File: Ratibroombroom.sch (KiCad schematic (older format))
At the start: 96 parts, among them J1 Conn_01x02_Male, J10 Conn_01x04_Male, J11 Conn_01x04_Male, J2 Conn_01x02_Male, J3 Conn_01x04_Male, J4 Conn_01x04_Male, J5 Conn_01x02_Male, J6 Conn_01x02_Male, J7 Conn_01x04_Male, J8 Conn_01x04_Male, J9 Conn_01x04_Male, Q1 IRLML6344, Q10 Q_NPN_BEC, Q2 IRLML6344, Q3 IRLML6344, Q4 IRLML6344, Q5 PT12-21B/TR8, Q6 PT12-21B/TR8, Q7 PT12-21B/TR8, Q8 PT12-21B/TR8, Q9 IRLML6344, SW1 B3U, SW2 B3U, U1 AZ1117-3.3, U2 DRV8835, U3 AS5145B-HSST, U4 MPU-9250, U5 STM32F405RGTx, U6 AS5145B-HSST, U7 DRV8835, Y1 8MHZ

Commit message: Add linear regulators to motor drivers supply. Include jumpers to select between direct (battery), regulated or none supply for the drivers.
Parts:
- added C28, C29, C30, C31: 10u, Capacitor_SMD:C_0603_1608Metric, symbol Device:C
- added JP1, JP2: Jumper_NC_Dual, Jumper:SolderJumper-3_P1.3mm_Open_RoundedPad1.0x1.5mm_NumberLabels, symbol Device:Jumper_NC_Dual
- added R28, R30: 5.6k, Resistor_SMD:R_0603_1608Metric, symbol Device:R
- added R29, R31: 1.8k, Resistor_SMD:R_0603_1608Metric, symbol Device:R
- added U8, U9: L6932D1.2TR, Package_SO:SO-8_5.3x6.2mm_P1.27mm, symbol schematic_sybmols:L6932D1.2TR
- C1, C10, C11, C12, C13, C14, C15, C16, C17, C18, C19, C2, C20, C21, C22, C23, C24, C25, C26, C27, C3, C4, C5, C6, C7, C8, C9: footprint (none) -> Capacitor_SMD:C_0603_1608Metric
- D1, D10, D7, D8, D9: footprint (none) -> LED_SMD:LED_0603_1608Metric
- R1, R10, R11, R12, R13, R14, R15, R16, R17, R18, R19, R2, R20, R21, R22, R23, R24, R25, R26, R27, R3, R4, R5, R6, R7, R8, R9: footprint (none) -> Resistor_SMD:R_0603_1608Metric
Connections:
- net labels added: FAN_MOTOR_1, FAN_MOTOR_2, V_MOTOR_L, V_MOTOR_R
- wire segments 343 -> 411
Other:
- moved on the sheet: C11, C12, C13, C14, C15, C16, C17, C18, C19, C20, C21, C22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

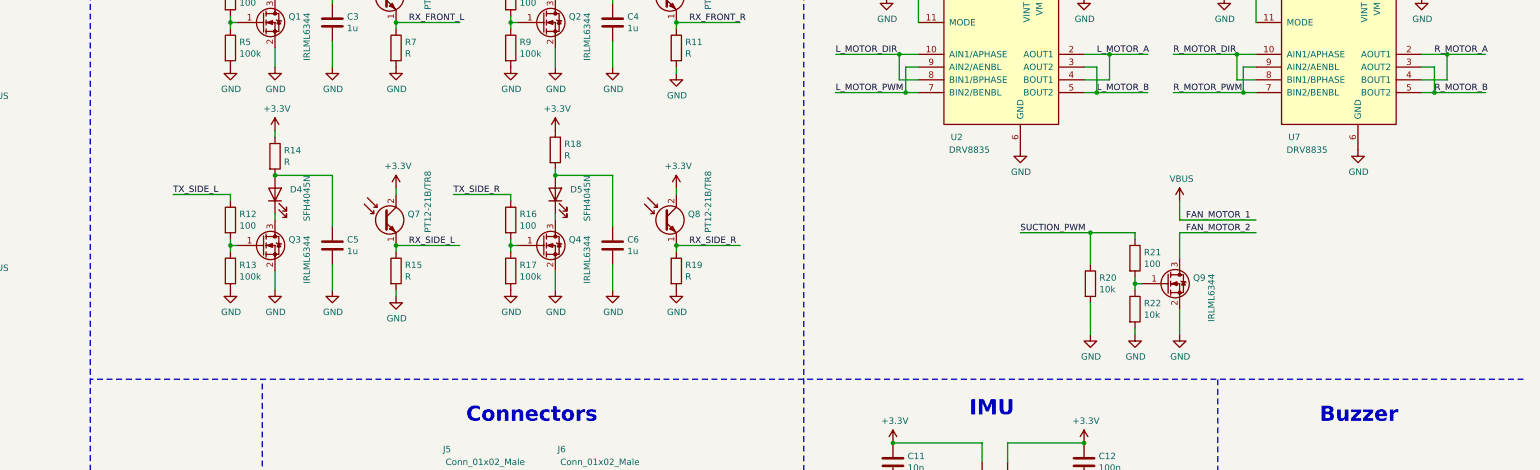
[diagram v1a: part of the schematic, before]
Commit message: Added pull-down resistors on motor pwm lines
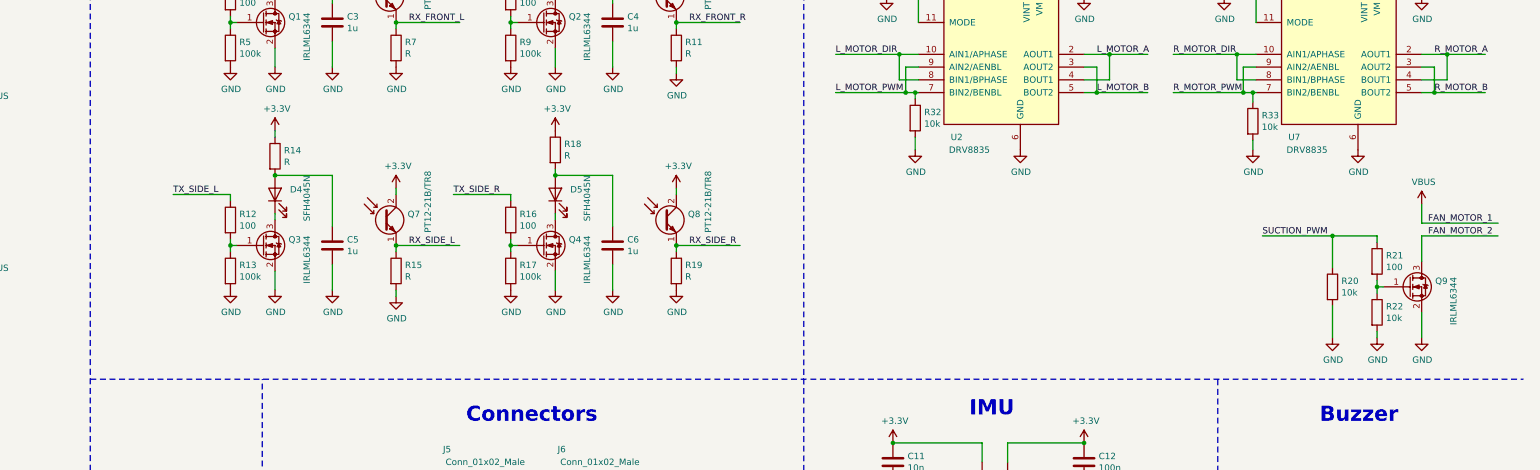
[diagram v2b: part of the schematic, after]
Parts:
- added R32, R33: 10k, Resistor_SMD:R_0603_1608Metric, symbol Device:R
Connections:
- wire segments 411 -> 417
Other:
- moved on the sheet: Q9, R20, R21, R22
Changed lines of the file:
@@
 EESchema Schematic File Version 4
 LIBS:Ratibroombroom-cache
-EELAYER 29 0
+EELAYER 26 0
 EELAYER END
 $Descr A3 16535 11693
@@
 L power:GND #PWR056
 U 1 1 5E51EE62
-P 12950 4300
-F 0 "#PWR056" H 12950 4050 50  0001 C CNN
-F 1 "GND" H 12955 4127 50  0000 C CNN
-F 2 "" H 12950 4300 50  0001 C CNN
-F 3 "" H 12950 4300 50  0001 C CNN
-	1    12950 4300
+P 14850 4325
+F 0 "#PWR056" H 14850 4075 50  0001 C CNN
+F 1 "GND" H 14855 4152 50  0000 C CNN
+F 2 "" H 14850 4325 50  0001 C CNN
+F 3 "" H 14850 4325 50  0001 C CNN
+	1    14850 4325
 	1    0    0    -1
 $EndComp
 Wire Wire Line
-	12950 3550 12950 3500
-Text Label 12050 3500 0    50   ~ 0
+	14850 3575 14850 3525
+Text Label 13950 3525 0    50   ~ 0
 SUCTION_PWM
 Wire Wire Line
-	12950 3900 12950 3850
-Connection ~ 12950 3900
+	14850 3925 14850 3875
+Connection ~ 14850 3925
 Wire Wire Line
-	13000 3900 12950 3900
+	14900 3925 14850 3925
 Wire Wire Line
-	12950 3950 12950 3900
+	14850 3975 14850 3925
 Wire Wire Line
-	13300 4100 13300 4300
+	15200 4125 15200 4325
 $Comp
 L power:GND #PWR058
 U 1 1 5E51EE81
-P 13300 4300
-F 0 "#PWR058" H 13300 4050 50  0001 C CNN
-F 1 "GND" H 13305 4127 50  0000 C CNN
-F 2 "" H 13300 4300 50  0001 C CNN
-F 3 "" H 13300 4300 50  0001 C CNN
-	1    13300 4300
+P 15200 4325
+F 0 "#PWR058" H 15200 4075 50  0001 C CNN
+F 1 "GND" H 15205 4152 50  0000 C CNN
+F 2 "" H 15200 4325 50  0001 C CNN
+F 3 "" H 15200 4325 50  0001 C CNN
+	1    15200 4325
 	1    0    0    -1
 $EndComp
@@
 L Device:R R21
 U 1 1 5E51EE8B
-P 12950 3700
-F 0 "R21" H 13020 3746 50  0000 L CNN
-F 1 "100" H 13020 3655 50  0000 L CNN
-F 2 "Resistor_SMD:R_0603_1608Metric" V 12880 3700 50  0001 C CNN
-F 3 "~" H 12950 3700 50  0001 C CNN
-	1    12950 3700
+P 14850 3725
+F 0 "R21" H 14920 3771 50  0000 L CNN
+F 1 "100" H 14920 3680 50  0000 L CNN
+F 2 "Resistor_SMD:R_0603_1608Metric" V 14780 3725 50  0001 C CNN
+F 3 "~" H 14850 3725 50  0001 C CNN
+	1    14850 3725
 	1    0    0    -1
 $EndComp
@@
 L Device:R R22
 U 1 1 5E51EE95
-P 12950 4100
-F 0 "R22" H 13020 4146 50  0000 L CNN
-F 1 "10k" H 13020 4055 50  0000 L CNN
-F 2 "Resistor_SMD:R_0603_1608Metric" V 12880 4100 50  0001 C CNN
-F 3 "~" H 12950 4100 50  0001 C CNN
-	1    12950 4100
+P 14850 4125
+F 0 "R22" H 14920 4171 50  0000 L CNN
+F 1 "10k" H 14920 4080 50  0000 L CNN
+F 2 "Resistor_SMD:R_0603_1608Metric" V 14780 4125 50  0001 C CNN
+F 3 "~" H 14850 4125 50  0001 C CNN
+	1    14850 4125
 	1    0    0    -1
 $EndComp
@@
 L Device:Q_NMOS_GSD Q9
 U 1 1 5E51EE9F
-P 13200 3900
-F 0 "Q9" H 13406 3946 50  0000 L CNN
-F 1 "IRLML6344" V 13550 3600 50  0000 L CNN
-F 2 "" H 13400 4000 50  0001 C CNN
-F 3 "~" H 13200 3900 50  0001 C CNN
-	1    13200 3900
+P 15100 3925
+F 0 "Q9" H 15306 3971 50  0000 L CNN
+F 1 "IRLML6344" V 15450 3625 50  0000 L CNN
+F 2 "" H 15300 4025 50  0001 C CNN
+F 3 "~" H 15100 3925 50  0001 C CNN
+	1    15100 3925
 	1    0    0    -1
 $EndComp
@@
 $EndComp
 Wire Wire Line
-	13900 3500 13300 3500
+	15800 3525 15200 3525
 Wire Wire Line
-	13300 3500 13300 3700
+	15200 3525 15200 3725
 Wire Wire Line
-	13900 3400 13300 3400
+	15800 3425 15200 3425
 Wire Wire Line
-	13300 3400 13300 3250
+	15200 3425 15200 3275
 $Comp
 L power:VBUS #PWR057
 U 1 1 5E53C651
-P 13300 3250
-F 0 "#PWR057" H 13300 3100 50  0001 C CNN
-F 1 "VBUS" H 13315 3423 50  0000 C CNN
-F 2 "" H 13300 3250 50  0001 C CNN
-F 3 "" H 13300 3250 50  0001 C CNN
-	1    13300 3250
+P 15200 3275
+F 0 "#PWR057" H 15200 3125 50  0001 C CNN
+F 1 "VBUS" H 15215 3448 50  0000 C CNN
+F 2 "" H 15200 3275 50  0001 C CNN
+F 3 "" H 15200 3275 50  0001 C CNN
+	1    15200 3275
 	1    0    0    -1
 $EndComp
@@
 L Device:R R20
 U 1 1 5E53FDF5
-P 12600 3900
-F 0 "R20" H 12670 3946 50  0000 L CNN
-F 1 "10k" H 12670 3855 50  0000 L CNN
-F 2 "Resistor_SMD:R_0603_1608Metric" V 12530 3900 50  0001 C CNN
-F 3 "~" H 12600 3900 50  0001 C CNN
-	1    12600 3900
+P 14500 3925
+F 0 "R20" H 14570 3971 50  0000 L CNN
+F 1 "10k" H 14570 3880 50  0000 L CNN
+F 2 "Resistor_SMD:R_0603_1608Metric" V 14430 3925 50  0001 C CNN
+F 3 "~" H 14500 3925 50  0001 C CNN
+	1    14500 3925
 	1    0    0    -1
 $EndComp
@@
 L power:GND #PWR055
 U 1 1 5E5400FA
-P 12600 4300
-F 0 "#PWR055" H 12600 4050 50  0001 C CNN
-F 1 "GND" H 12605 4127 50  0000 C CNN
-F 2 "" H 12600 4300 50  0001 C CNN
-F 3 "" H 12600 4300 50  0001 C CNN
-	1    12600 4300
+P 14500 4325
+F 0 "#PWR055" H 14500 4075 50  0001 C CNN
+F 1 "GND" H 14505 4152 50  0000 C CNN
+F 2 "" H 14500 4325 50  0001 C CNN
+F 3 "" H 14500 4325 50  0001 C CNN
+	1    14500 4325
 	1    0    0    -1
 $EndComp
-Wire Wire Line
-	12050 3500 12600 3500
-Wire Wire Line
-	12600 3750 12600 3500
-Connection ~ 12600 3500
-Wire Wire Line
-	12600 3500 12950 3500
 $Comp
 L Device:LED D7
@@
 	7150 3950 7150 4000
 Wire Wire Line
-	12950 4250 12950 4300
+	14850 4275 14850 4325
 Wire Wire Line
-	12600 4050 12600 4300
+	14500 4075 14500 4325
 $Comp
 L Connector:Conn_01x04_Male J7
@@
 Wire Wire Line
 	9250 7250 8700 7250
-Text Label 13350 3400 0    50   ~ 0
+Text Label 15250 3425 0    50   ~ 0
 FAN_MOTOR_1
-Text Label 13350 3500 0    50   ~ 0
+Text Label 15250 3525 0    50   ~ 0
 FAN_MOTOR_2
 $Comp
@@
 	11150 2200 11150 2400
 Wire Wire Line
-	11150 2400 11250 2400
+	11150 2400 11225 2400
 Wire Wire Line
 	11150 2400 10600 2400
@@
 	13800 2200 13800 2400
 Wire Wire Line
-	13800 2400 13900 2400
+	13800 2400 13875 2400
 Wire Wire Line
 	13800 2400 13250 2400
 Connection ~ 13800 2400
 Wire Notes Line width 12
-	16000 4650 10350 4650
-Wire Notes Line width 12
 	10350 7450 16050 7450
 Wire Notes Line width 12
@@
 	10350 500  10350 11200
 Wire Notes Line
-	10350 4650 4750 4650
-Wire Notes Line
 	4750 5450 500  5450
 Wire Notes Line
@@
 Wire Notes Line
 	6100 8650 6100 4650
+Wire Notes Line
+	4750 4650 16000 4650
+Wire Wire Line
+	14500 3775 14500 3525
+Connection ~ 14500 3525
+Wire Wire Line
+	14500 3525 14850 3525
+Wire Wire Line
+	13950 3525 14500 3525
+$Comp
+L Device:R R33
+U 1 1 5E2DCD69
+P 13875 2625
+F 0 "R33" H 13945 2671 50  0000 L CNN
+F 1 "10k" H 13945 2580 50  0000 L CNN
+F 2 "Resistor_SMD:R_0603_1608Metric" V 13805 2625 50  0001 C CNN
+F 3 "~" H 13875 2625 50  0001 C CNN
+	1    13875 2625
+	1    0    0    -1
+$EndComp
+$Comp
+L Device:R R32
+U 1 1 5E2DCFAB
+P 11225 2600
+F 0 "R32" H 11295 2646 50  0000 L CNN
+F 1 "10k" H 11295 2555 50  0000 L CNN
+F 2 "Resistor_SMD:R_0603_1608Metric" V 11155 2600 50  0001 C CNN
+F 3 "~" H 11225 2600 50  0001 C CNN
+	1    11225 2600
+	1    0    0    -1
+$EndComp
+$Comp
+L power:GND #PWR092
+U 1 1 5E2DD0D3
+P 13875 2850
+F 0 "#PWR092" H 13875 2600 50  0001 C CNN
+F 1 "GND" H 13880 2677 50  0000 C CNN
+F 2 "" H 13875 2850 50  0001 C CNN
+F 3 "" H 13875 2850 50  0001 C CNN
+	1    13875 2850
+	1    0    0    -1
+$EndComp
+$Comp
+L power:GND #PWR091
+U 1 1 5E2DD1BA
+P 11225 2850
+F 0 "#PWR091" H 11225 2600 50  0001 C CNN
+F 1 "GND" H 11230 2677 50  0000 C CNN
+F 2 "" H 11225 2850 50  0001 C CNN
+F 3 "" H 11225 2850 50  0001 C CNN
+	1    11225 2850
+	1    0    0    -1
+$EndComp
+Wire Wire Line
+	11225 2450 11225 2400
+Connection ~ 11225 2400
+Wire Wire Line
+	11225 2400 11250 2400
+Wire Wire Line
+	11225 2750 11225 2850
+Wire Wire Line
+	13875 2475 13875 2400
+Connection ~ 13875 2400
+Wire Wire Line
+	13875 2400 13900 2400
+Wire Wire Line
+	13875 2850 13875 2775
 $EndSCHEMATC

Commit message: Added comments in schematics
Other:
- note added: "C3, C4, C5, C6\nteñen que ir ahí \nou a 3V3.\nComentar"
- note added: "Engadín R32 e R33 para que\nen caso de 3º estado os nos \npines do micro, non se activen\nos motores"
- note added: "JP1 e JP2:\nse poden quedar\nabertos, valen \npara desconectar\nmotores"
- note added: "Por qué?"
- note added: "R28, R29, R30, R31\nque sexan do 1% \nou mellor para que\nnon se desbalanceen\nas tensións dos motores"
- moved on the sheet: Q9, R20, R21, R22
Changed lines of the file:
@@
 L power:GND #PWR056
 U 1 1 5E51EE62
-P 14850 4325
-F 0 "#PWR056" H 14850 4075 50  0001 C CNN
-F 1 "GND" H 14855 4152 50  0000 C CNN
-F 2 "" H 14850 4325 50  0001 C CNN
-F 3 "" H 14850 4325 50  0001 C CNN
-	1    14850 4325
-	1    0    0    -1
-$EndComp
-Wire Wire Line
-	14850 3575 14850 3525
-Text Label 13950 3525 0    50   ~ 0
+P 13000 4300
+F 0 "#PWR056" H 13000 4050 50  0001 C CNN
+F 1 "GND" H 13005 4127 50  0000 C CNN
+F 2 "" H 13000 4300 50  0001 C CNN
+F 3 "" H 13000 4300 50  0001 C CNN
+	1    13000 4300
+	1    0    0    -1
+$EndComp
+Wire Wire Line
+	13000 3550 13000 3500
+Text Label 12100 3500 0    50   ~ 0
 SUCTION_PWM
 Wire Wire Line
-	14850 3925 14850 3875
-Connection ~ 14850 3925
-Wire Wire Line
-	14900 3925 14850 3925
-Wire Wire Line
-	14850 3975 14850 3925
-Wire Wire Line
-	15200 4125 15200 4325
+	13000 3900 13000 3850
+Connection ~ 13000 3900
+Wire Wire Line
+	13050 3900 13000 3900
+Wire Wire Line
+	13000 3950 13000 3900
+Wire Wire Line
+	13350 4100 13350 4300
 $Comp
 L power:GND #PWR058
 U 1 1 5E51EE81
-P 15200 4325
-F 0 "#PWR058" H 15200 4075 50  0001 C CNN
-F 1 "GND" H 15205 4152 50  0000 C CNN
-F 2 "" H 15200 4325 50  0001 C CNN
-F 3 "" H 15200 4325 50  0001 C CNN
-	1    15200 4325
+P 13350 4300
+F 0 "#PWR058" H 13350 4050 50  0001 C CNN
+F 1 "GND" H 13355 4127 50  0000 C CNN
+F 2 "" H 13350 4300 50  0001 C CNN
+F 3 "" H 13350 4300 50  0001 C CNN
+	1    13350 4300
 	1    0    0    -1
 $EndComp
@@
 L Device:R R21
 U 1 1 5E51EE8B
-P 14850 3725
-F 0 "R21" H 14920 3771 50  0000 L CNN
-F 1 "100" H 14920 3680 50  0000 L CNN
-F 2 "Resistor_SMD:R_0603_1608Metric" V 14780 3725 50  0001 C CNN
-F 3 "~" H 14850 3725 50  0001 C CNN
-	1    14850 3725
+P 13000 3700
+F 0 "R21" H 13070 3746 50  0000 L CNN
+F 1 "100" H 13070 3655 50  0000 L CNN
+F 2 "Resistor_SMD:R_0603_1608Metric" V 12930 3700 50  0001 C CNN
+F 3 "~" H 13000 3700 50  0001 C CNN
+	1    13000 3700
 	1    0    0    -1
 $EndComp
@@
 L Device:R R22
 U 1 1 5E51EE95
-P 14850 4125
-F 0 "R22" H 14920 4171 50  0000 L CNN
-F 1 "10k" H 14920 4080 50  0000 L CNN
-F 2 "Resistor_SMD:R_0603_1608Metric" V 14780 4125 50  0001 C CNN
-F 3 "~" H 14850 4125 50  0001 C CNN
-	1    14850 4125
+P 13000 4100
+F 0 "R22" H 13070 4146 50  0000 L CNN
+F 1 "10k" H 13070 4055 50  0000 L CNN
+F 2 "Resistor_SMD:R_0603_1608Metric" V 12930 4100 50  0001 C CNN
+F 3 "~" H 13000 4100 50  0001 C CNN
+	1    13000 4100
 	1    0    0    -1
 $EndComp
@@
 L Device:Q_NMOS_GSD Q9
 U 1 1 5E51EE9F
-P 15100 3925
-F 0 "Q9" H 15306 3971 50  0000 L CNN
-F 1 "IRLML6344" V 15450 3625 50  0000 L CNN
-F 2 "" H 15300 4025 50  0001 C CNN
-F 3 "~" H 15100 3925 50  0001 C CNN
-	1    15100 3925
+P 13250 3900
+F 0 "Q9" H 13456 3946 50  0000 L CNN
+F 1 "IRLML6344" V 13600 3600 50  0000 L CNN
+F 2 "" H 13450 4000 50  0001 C CNN
+F 3 "~" H 13250 3900 50  0001 C CNN
+	1    13250 3900
 	1    0    0    -1
 $EndComp
@@
 $EndComp
 Wire Wire Line
-	15800 3525 15200 3525
-Wire Wire Line
-	15200 3525 15200 3725
-Wire Wire Line
-	15800 3425 15200 3425
-Wire Wire Line
-	15200 3425 15200 3275
+	13950 3500 13350 3500
+Wire Wire Line
+	13350 3500 13350 3700
+Wire Wire Line
+	13950 3400 13350 3400
+Wire Wire Line
+	13350 3400 13350 3250
 $Comp
 L power:VBUS #PWR057
 U 1 1 5E53C651
-P 15200 3275
-F 0 "#PWR057" H 15200 3125 50  0001 C CNN
-F 1 "VBUS" H 15215 3448 50  0000 C CNN
-F 2 "" H 15200 3275 50  0001 C CNN
-F 3 "" H 15200 3275 50  0001 C CNN
-	1    15200 3275
+P 13350 3250
+F 0 "#PWR057" H 13350 3100 50  0001 C CNN
+F 1 "VBUS" H 13365 3423 50  0000 C CNN
+F 2 "" H 13350 3250 50  0001 C CNN
+F 3 "" H 13350 3250 50  0001 C CNN
+	1    13350 3250
 	1    0    0    -1
 $EndComp
@@
 L Device:R R20
 U 1 1 5E53FDF5
-P 14500 3925
-F 0 "R20" H 14570 3971 50  0000 L CNN
-F 1 "10k" H 14570 3880 50  0000 L CNN
-F 2 "Resistor_SMD:R_0603_1608Metric" V 14430 3925 50  0001 C CNN
-F 3 "~" H 14500 3925 50  0001 C CNN
-	1    14500 3925
+P 12650 3900
+F 0 "R20" H 12720 3946 50  0000 L CNN
+F 1 "10k" H 12720 3855 50  0000 L CNN
+F 2 "Resistor_SMD:R_0603_1608Metric" V 12580 3900 50  0001 C CNN
+F 3 "~" H 12650 3900 50  0001 C CNN
+	1    12650 3900
 	1    0    0    -1
 $EndComp
@@
 L power:GND #PWR055
 U 1 1 5E5400FA
-P 14500 4325
-F 0 "#PWR055" H 14500 4075 50  0001 C CNN
-F 1 "GND" H 14505 4152 50  0000 C CNN
-F 2 "" H 14500 4325 50  0001 C CNN
-F 3 "" H 14500 4325 50  0001 C CNN
-	1    14500 4325
+P 12650 4300
+F 0 "#PWR055" H 12650 4050 50  0001 C CNN
+F 1 "GND" H 12655 4127 50  0000 C CNN
+F 2 "" H 12650 4300 50  0001 C CNN
+F 3 "" H 12650 4300 50  0001 C CNN
+	1    12650 4300
 	1    0    0    -1
 $EndComp
@@
 	7150 3950 7150 4000
 Wire Wire Line
-	14850 4275 14850 4325
-Wire Wire Line
-	14500 4075 14500 4325
+	13000 4250 13000 4300
+Wire Wire Line
+	12650 4050 12650 4300
 $Comp
 L Connector:Conn_01x04_Male J7
@@
 Wire Wire Line
 	9250 7250 8700 7250
-Text Label 15250 3425 0    50   ~ 0
+Text Label 13400 3400 0    50   ~ 0
 FAN_MOTOR_1
-Text Label 15250 3525 0    50   ~ 0
+Text Label 13400 3500 0    50   ~ 0
 FAN_MOTOR_2
 $Comp
@@
 	4750 4650 16000 4650
 Wire Wire Line
-	14500 3775 14500 3525
-Connection ~ 14500 3525
-Wire Wire Line
-	14500 3525 14850 3525
-Wire Wire Line
-	13950 3525 14500 3525
+	12650 3750 12650 3500
+Connection ~ 12650 3500
+Wire Wire Line
+	12650 3500 13000 3500
+Wire Wire Line
+	12100 3500 12650 3500
 $Comp
 L Device:R R33
@@
 Wire Wire Line
 	13875 2850 13875 2775
+Text Notes 3800 3650 0    50   ~ 0
+R28, R29, R30, R31\nque sexan do 1% \nou mellor para que\nnon se desbalanceen\nas tensións dos motores
+Text Notes 875  2975 0    50   ~ 0
+JP1 e JP2:\nse poden quedar\nabertos, valen \npara desconectar\nmotores
+Text Notes 6800 2825 0    50   ~ 0
+C3, C4, C5, C6\nteñen que ir ahí \nou a 3V3.\nComentar
+Text Notes 12475 2875 0    50   ~ 0
+Engadín R32 e R33 para que\nen caso de 3º estado os nos \npines do micro, non se activen\nos motores
+Text Notes 3875 8675 0    50   ~ 0
+Por qué?
 $EndSCHEMATC

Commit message: More comments on schematics
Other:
- note added: "Comentar cómo se vai\na integrar a PCB principal\ncoas dos encoders"
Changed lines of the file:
@@
 Text Notes 3875 8675 0    50   ~ 0
 Por qué?
+Text Notes 10000 8275 0    50   ~ 0
+Comentar cómo se vai\na integrar a PCB principal\ncoas dos encoders
 $EndSCHEMATC

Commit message: Typo fix
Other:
- note added: "Engadín R32 e R33 para que\nen caso de 3º estado nos \npines do micro, non se activen\nos motores"
- note removed: "Engadín R32 e R33 para que\nen caso de 3º estado os nos \npines do micro, non se activen\nos motores"
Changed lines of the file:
@@
 C3, C4, C5, C6\nteñen que ir ahí \nou a 3V3.\nComentar
 Text Notes 12475 2875 0    50   ~ 0
-Engadín R32 e R33 para que\nen caso de 3º estado os nos \npines do micro, non se activen\nos motores
+Engadín R32 e R33 para que\nen caso de 3º estado nos \npines do micro, non se activen\nos motores
 Text Notes 3875 8675 0    50   ~ 0
 Por qué?

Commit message: Modify connection of capacitors in IR emitters. Add on/of switch through mosfet. Assign footprints to every schematic symbol.
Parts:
- added Q11: IRF7416PbF, Package_SO:SO-8_5.3x6.2mm_P1.27mm, symbol schematic_sybmols:IRF7416PbF
- added R34: 10k, Resistor_SMD:R_0603_1608Metric, symbol Device:R
- added SW3: PCM12, Button_Switch_SMD:SW_SPDT_PCM12, symbol Switch:SW_DPDT_x2
- BZ1: footprint (none) -> Ratibroombroom:MLT-5020
- D2, D3, D4, D5: footprint (none) -> Ratibroombroom:SFH4045N
- D6: value 1N141B -> 1N1418; footprint (none) -> Diode_SMD:D_SOD-323
- J1: footprint (none) -> Connector_JST:JST_XH_B2B-XH-A_1x02_P2.50mm_Vertical
- J10, J11: footprint (none) -> Ratibroombroom:Edge_connector_4P_1x3mm
- J2, J5, J6: footprint (none) -> Ratibroombroom:Pad_SMD_2P_1x3mm
- J3, J4, J7: footprint (none) -> Connector_PinHeader_2.54mm:PinHeader_1x04_P2.54mm_Vertical
- J8, J9: footprint (none) -> Ratibroombroom:Pad_SMD_4P_1x3mm
- Q1, Q2, Q3, Q4, Q9: footprint (none) -> Package_TO_SOT_SMD:SOT-23
- Q10: value Q_NPN_BEC -> S8050; footprint (none) -> Package_TO_SOT_SMD:SOT-23
- Q5, Q6, Q7, Q8: footprint (none) -> Ratibroombroom:PT12-21B-TR8
- SW1, SW2: footprint (none) -> Button_Switch_SMD:SW_SPST_B3U-1000P
- U1: footprint (none) -> Package_TO_SOT_SMD:SOT-223-3_TabPin2
- U3, U6: footprint (none) -> Package_SO:SSOP-16_5.3x6.2mm_P0.65mm
- Y1: footprint (none) -> Crystal:Crystal_SMD_5032-4Pin_5.0x3.2mm
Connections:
- wire segments 417 -> 423
- no-connect marks 28 -> 29
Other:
- note removed: "C3, C4, C5, C6\nteñen que ir ahí \nou a 3V3.\nComentar"
- note removed: "Engadín R32 e R33 para que\nen caso de 3º estado nos \npines do micro, non se activen\nos motores"
- note removed: "Por qué?"
- moved on the sheet: C1, C2, D1, J1, R1, R18, R2, R3, U1
